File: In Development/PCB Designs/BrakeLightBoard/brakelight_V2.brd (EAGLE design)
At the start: 68.6 x 38.1 mm, 14 parts, among them Q2 30N06L

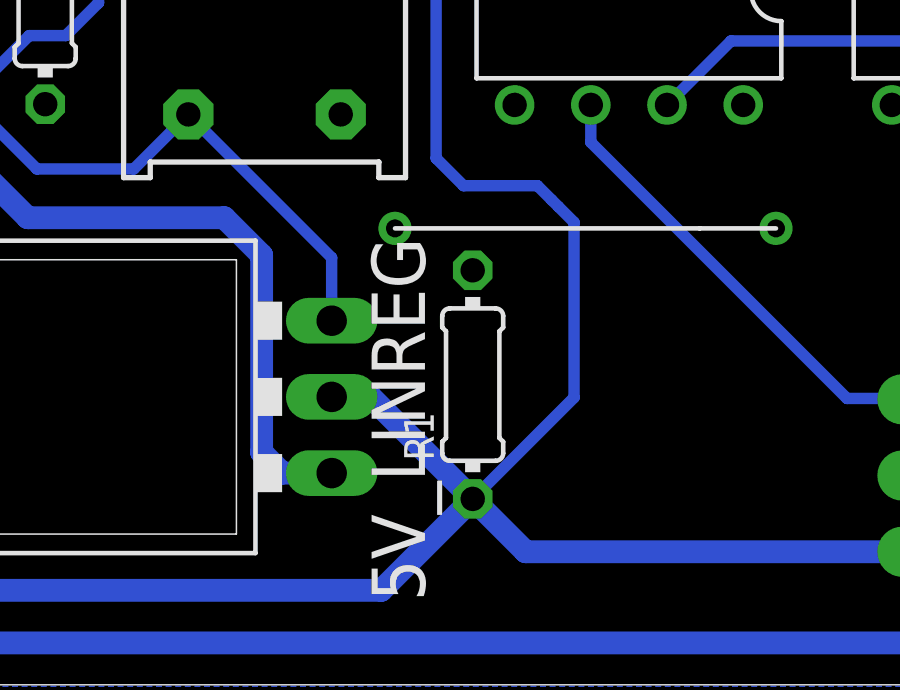
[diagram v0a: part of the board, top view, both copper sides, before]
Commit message: Fixed flaw in brakelight v2
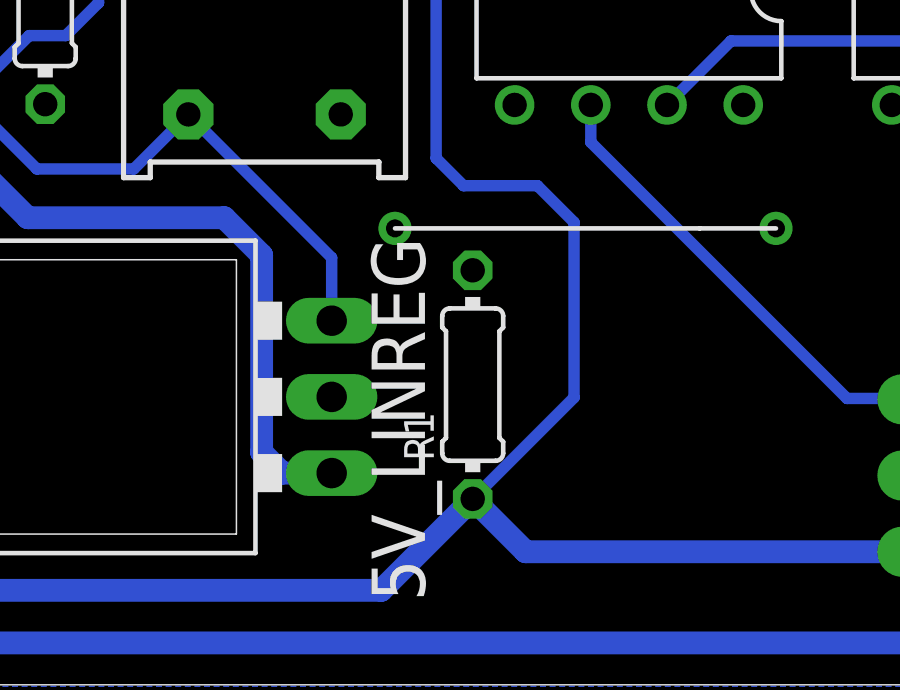
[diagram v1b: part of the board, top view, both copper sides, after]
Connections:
- net 0V: now also 5V_LINREG.GND
- net V-: no longer 5V_LINREG.GND
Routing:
- net V-: track 111.3 -> 105.2 mm
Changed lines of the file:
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@@
 <contactref element="U$4" pad="P$1"/>
 <contactref element="U$4" pad="P$2"/>
-<wire x1="39.4716" y1="15.2146" x2="29.3624" y2="13.8176" width="0" layer="19" extent="1-1"/>
+<contactref element="5V_LINREG" pad="GND"/>
+<wire x1="39.4716" y1="15.2146" x2="62.1676" y2="16.7394" width="0" layer="19" extent="1-1"/>
+<wire x1="29.3624" y1="13.8176" x2="39.4716" y2="15.2146" width="0" layer="19" extent="1-1"/>
+<wire x1="26.7716" y1="15.2146" x2="29.3624" y2="13.8176" width="0" layer="19" extent="1-1"/>
+<wire x1="24.9642" y1="19.0142" x2="26.7716" y2="15.2146" width="0" layer="19" extent="1-1"/>
+<wire x1="24.6612" y1="9.5976" x2="26.7716" y2="15.2146" width="0" layer="19" extent="1-1"/>
+<wire x1="15.113" y1="19.3548" x2="24.9642" y2="19.0142" width="0" layer="19" extent="1-1"/>
+<wire x1="26.8802" y1="32.3986" x2="24.9642" y2="19.0142" width="0" layer="19" extent="1-1"/>
+<wire x1="42.9332" y1="32.4626" x2="26.8802" y2="32.3986" width="0" layer="19" extent="1-1"/>
 </signal>
 <signal name="V-">
@@
 <contactref element="R1" pad="1"/>
 <contactref element="LIPO_CONN" pad="2"/>
-<contactref element="5V_LINREG" pad="GND"/>
 <wire x1="34.5186" y1="23.5204" x2="31.0896" y2="26.9494" width="0.381" layer="16"/>
 <wire x1="30.7594" y1="26.9494" x2="31.0896" y2="26.9494" width="0.381" layer="16"/>
@@
 <wire x1="26.3144" y1="3.1496" x2="29.3624" y2="6.1976" width="0.762" layer="16"/>
 <wire x1="3.7846" y1="20.167" x2="3.7846" y2="4.9276" width="0.762" layer="16"/>
-<wire x1="24.6612" y1="9.5976" x2="25.9624" y2="9.5976" width="0.762" layer="16"/>
-<wire x1="25.9624" y1="9.5976" x2="29.3624" y2="6.1976" width="0.762" layer="16"/>
 <wire x1="29.3624" y1="6.1976" x2="31.1244" y2="4.4356" width="0.762" layer="16"/>
 <wire x1="31.1244" y1="4.4356" x2="44.5262" y2="4.4356" width="0.762" layer="16"/>
@@
 <wire x1="28.1432" y1="17.5514" x2="29.0576" y2="16.637" width="0.381" layer="16"/>
 <wire x1="29.0576" y1="16.637" x2="31.5214" y2="16.637" width="0.381" layer="16"/>
-<wire x1="31.5214" y1="16.637" x2="31.9913" y2="16.1671" width="0.381" layer="16"/>
-<wire x1="31.9913" y1="16.1671" x2="32.2199" y2="15.9385" width="0.381" layer="16"/>
-<wire x1="32.2199" y1="15.9385" x2="32.7406" y2="15.4178" width="0.381" layer="16"/>
+<wire x1="31.5214" y1="16.637" x2="32.7406" y2="15.4178" width="0.381" layer="16"/>
 <wire x1="32.7406" y1="9.5758" x2="29.3624" y2="6.1976" width="0.381" layer="16"/>
 <wire x1="28.1432" y1="24.3332" x2="28.1432" y2="17.5514" width="0.381" layer="16"/>
